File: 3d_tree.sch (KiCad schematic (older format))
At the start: 0 parts

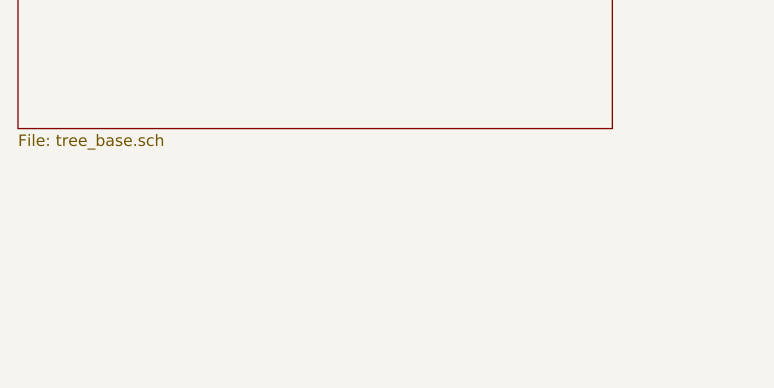
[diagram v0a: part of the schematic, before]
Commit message: Add USB variant; update to use 3xAAA
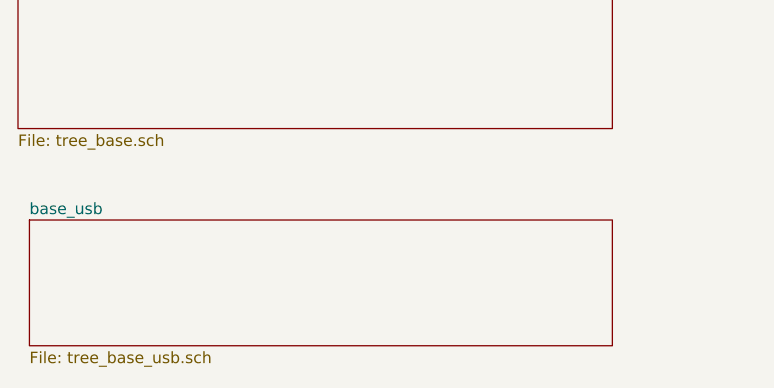
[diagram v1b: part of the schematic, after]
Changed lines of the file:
@@
 $Descr A4 11693 8268
 encoding utf-8
-Sheet 1 4
+Sheet 1 8
 Title ""
 Date ""
@@
 F1 "tree_display.sch" 50
 $EndSheet
+$Sheet
+S 1150 2250 2550 550
+U 5FDBD20E
+F0 "base_usb" 50
+F1 "tree_base_usb.sch" 50
+$EndSheet
 $EndSCHEMATC
